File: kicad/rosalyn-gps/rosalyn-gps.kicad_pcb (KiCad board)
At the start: 4 copper layers, 45 x 20 mm, 27 parts, among them J1 GpsMag, J2 SMA, U1 MIC5219-3.3YM5, U2 NEO-M8M, U3 24LC32, U4 HSCDTD008A, U5 HMC5883L

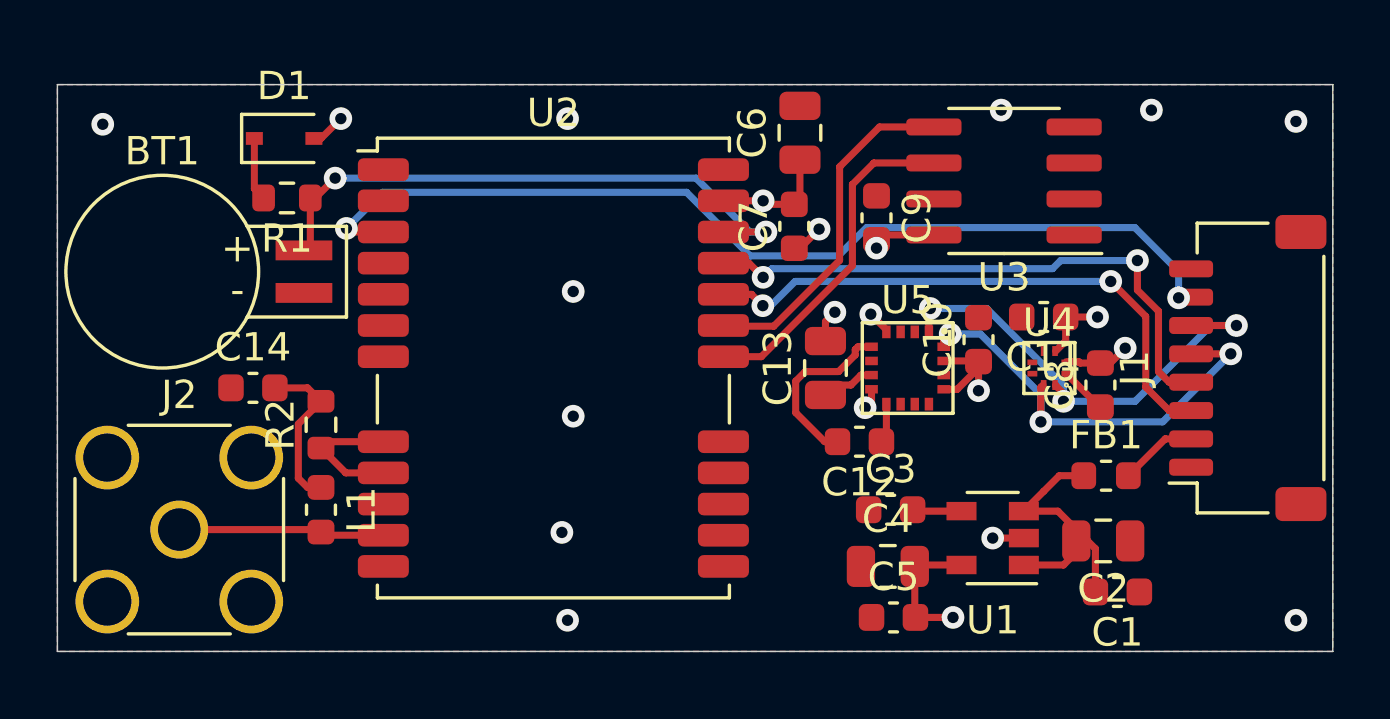
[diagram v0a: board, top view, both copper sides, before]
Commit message: cleanup pcb layout
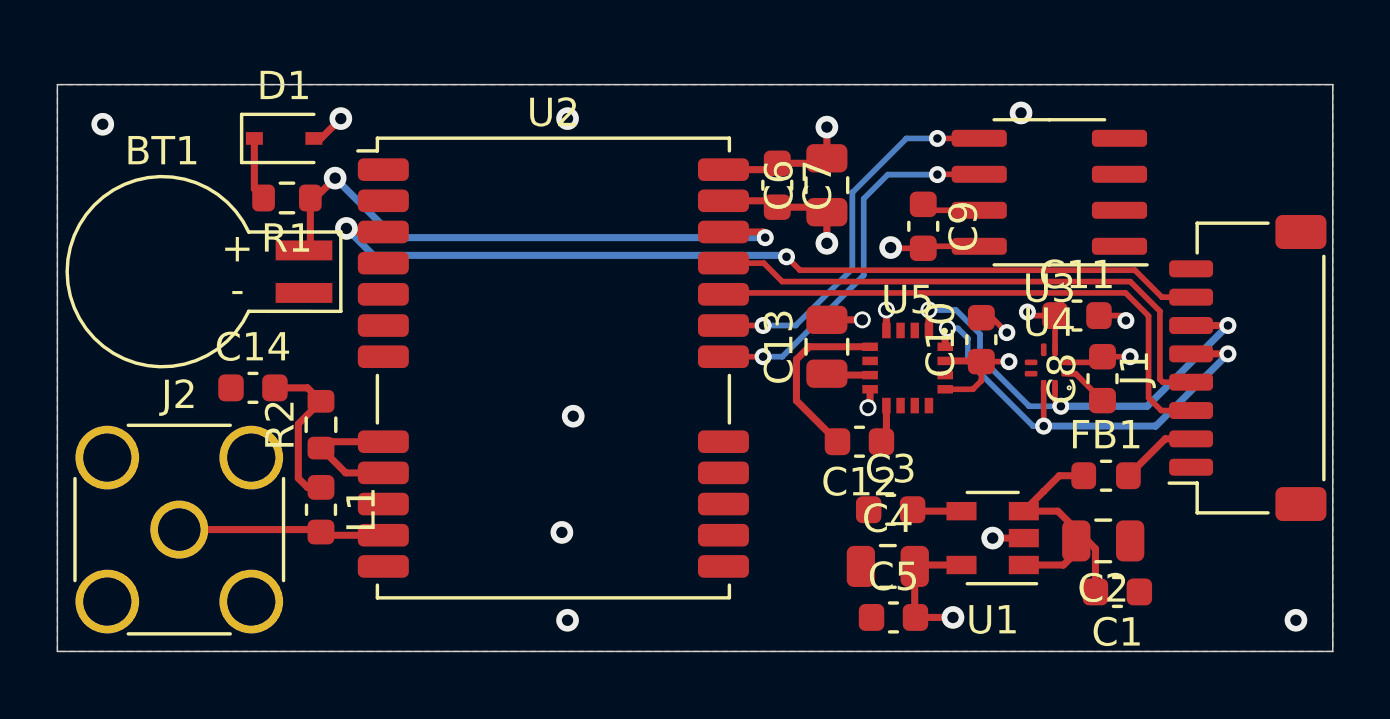
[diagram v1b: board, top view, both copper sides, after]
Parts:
- moved C6 2.08 mm to (147.2, 113.5)
- moved C9 1.68 mm to (150.6, 115.0)
- moved U3 1.65 mm to (155.0, 113.8)
- moved C7 1.57 mm to (145.4, 113.5), turned to 270 degrees
- moved C11 1.18 mm to (156.0, 118.2), turned to 0 degrees
- moved C13 0.75 mm to (147.2, 119.2)
- moved C8 0.24 mm to (156.9, 120.4)
- moved C10 0.10 mm to (152.6, 119.0)
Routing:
- net GND: track 6.68 -> 14.5 mm, vias 15 -> 14
- net gps_pps: track 35.0 -> 32.5 mm
- net +3V3: track 21.5 -> 23.1 mm
- net gps_scl: track 11.9 -> 13.3 mm, vias 0 -> 2
- net gps_sda: track 12.3 -> 13.3 mm, vias 0 -> 2
- net gps_rx: track 20.6 -> 19.6 mm, vias 2 -> 0
- net gps_tx: track 20.4 -> 19.9 mm, vias 2 -> 0
